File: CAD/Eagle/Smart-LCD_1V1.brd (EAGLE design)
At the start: 99 x 67.7 mm, 49 parts, among them Q121 MMBT2222AL, U101 MEGA8-P, U221 MCP4018T-104E/LT, U401 TS4871ID, X131 LDR, X141 Switches, X151 LEDs, X201 LCD_23WAY__UC1608, X231 LED_A, X232 LED_K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

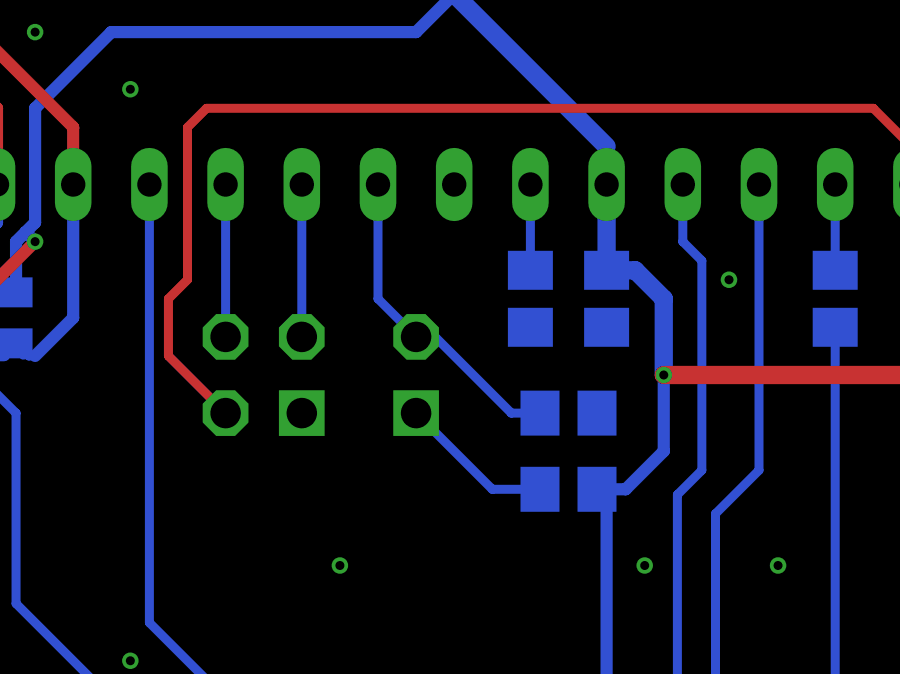
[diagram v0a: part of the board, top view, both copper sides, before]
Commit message: CAD - new version V1.1 - missing resistor for LDR added, missing header pin number 1 marking added
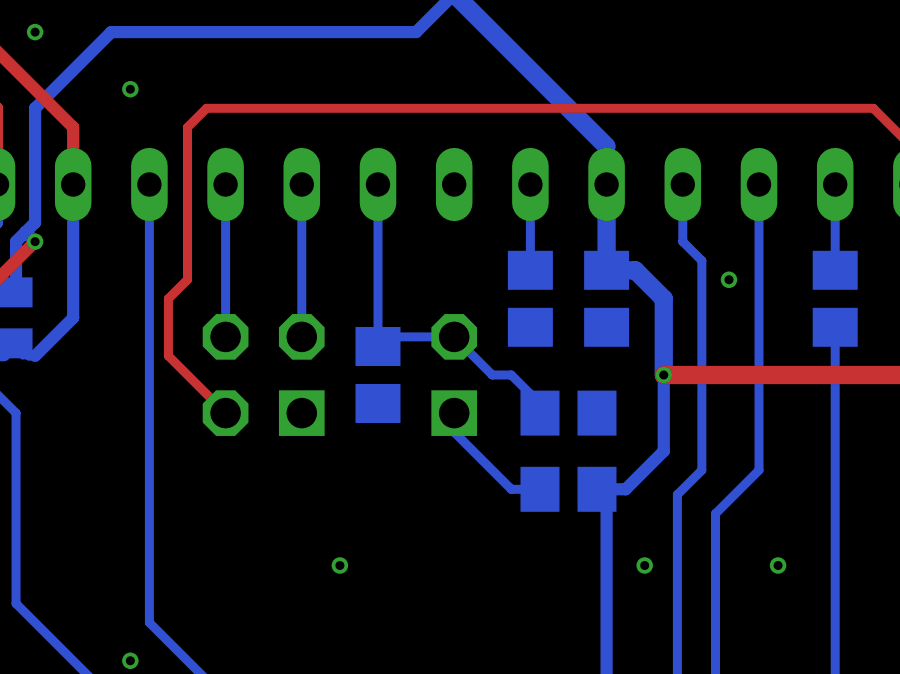
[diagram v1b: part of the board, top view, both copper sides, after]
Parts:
- added R132: 5.6kR, rcl:R0805
- moved X131 1.27 mm to (48.3, 26.0)
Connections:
- net GND: now also R132.2
- net LDR: now also R132.1
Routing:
- net LDR_P: track 5.18 -> 4.28 mm
- net LDR: track 10.8 -> 11.7 mm
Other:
- board text added: "1"
- board text added: "Smart-LCD V1.1 by DF4IAH"
- board text removed: "Smart-LCD V1.0 by DF4IAH"
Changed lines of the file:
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@@
 <dimension x1="0" y1="0" x2="0" y2="67.7" x3="-8.5" y3="33.85" textsize="1.016" layer="47"/>
 <dimension x1="0" y1="67.7" x2="99" y2="67.7" x3="49.5" y3="76.015" textsize="1.016" layer="47"/>
-<text x="27.94" y="62.865" size="1.4224" layer="22" ratio="15" rot="MR0">Smart-LCD V1.0
+<text x="27.94" y="62.865" size="1.4224" layer="22" ratio="15" rot="MR0">Smart-LCD V1.1
 by DF4IAH</text>
 <text x="48.26" y="22.86" size="1.016" layer="26" ratio="12" rot="MR0">LDR</text>
@@
 <dimension x1="0" y1="0" x2="0" y2="7.5" x3="-3.5" y3="3.75" textsize="0.6096" layer="47"/>
 <text x="97.155" y="29.845" size="1.016" layer="26" ratio="12" rot="MR0">Audio</text>
+<text x="52.07" y="65.405" size="0.6096" layer="22" ratio="20" rot="MR0">1</text>
+<text x="39.37" y="59.69" size="0.6096" layer="22" ratio="20" rot="MR0">1</text>
+<text x="92.71" y="36.83" size="0.6096" layer="22" ratio="20" rot="MR0">1</text>
+<text x="49.53" y="24.13" size="0.6096" layer="22" ratio="20" rot="MR0">1</text>
+<text x="43.815" y="24.13" size="0.6096" layer="22" ratio="20" rot="MR0">1</text>
 </plain>
 <attributes>
@@
 </class>
 </classes>
-<designrules name="Smart-LCD_1V0 *">
+<designrules name="Smart-LCD_1V1">
 <description language="de">
 &lt;p&gt;
@@
 </element>
 <element name="R222" library="rcl" package="R0805" value="650kR" x="30.48" y="24.765" smashed="yes" rot="MR0">
-<attribute name="NAME" x="34.925" y="24.765" size="0.6096" layer="26" rot="MR0"/>
+<attribute name="NAME" x="31.75" y="22.86" size="0.6096" layer="26" rot="MR0"/>
 <attribute name="VALUE" x="31.75" y="24.13" size="0.6096" layer="28" rot="MR0"/>
 </element>
@@
 </element>
 <element name="C102" library="rcl" package="C0805" value="100nF" x="53.34" y="29.845" smashed="yes" rot="MR270">
-<attribute name="NAME" x="54.61" y="27.94" size="0.6096" layer="26" rot="MR90"/>
+<attribute name="NAME" x="54.61" y="28.575" size="0.6096" layer="26" rot="MR90"/>
 <attribute name="VALUE" x="53.975" y="31.115" size="0.6096" layer="28" rot="MR270"/>
 </element>
@@
 <attribute name="VALUE" x="73.025" y="0.635" size="0.6096" layer="28" rot="MR90"/>
 </element>
-<element name="X131" library="df4iah_connector" package="1X02" value="LDR" x="46.99" y="26.035" smashed="yes" rot="MR0">
+<element name="X131" library="df4iah_connector" package="1X02" value="LDR" x="48.26" y="26.035" smashed="yes" rot="MR0">
 <attribute name="NAME" x="48.26" y="30.48" size="1.016" layer="26" ratio="10" rot="MR0"/>
-<attribute name="VALUE" x="46.99" y="27.94" size="0.6096" layer="28" rot="MR270"/>
+<attribute name="VALUE" x="48.26" y="27.94" size="0.6096" layer="28" rot="MR270"/>
 </element>
 <element name="R131" library="rcl" package="R0805" value="33kR" x="52.07" y="23.495" smashed="yes" rot="MR0">
-<attribute name="NAME" x="53.975" y="21.59" size="0.6096" layer="26" rot="MR0"/>
+<attribute name="NAME" x="53.34" y="21.59" size="0.6096" layer="26" rot="MR0"/>
 <attribute name="VALUE" x="53.34" y="22.86" size="0.6096" layer="28" rot="MR0"/>
 </element>
@@
 </element>
 <element name="X141" library="df4iah_connector" package="2X02" value="Switches" x="41.91" y="27.305" smashed="yes" rot="MR0">
-<attribute name="NAME" x="43.815" y="30.48" size="1.016" layer="26" ratio="10" rot="MR0"/>
+<attribute name="NAME" x="43.18" y="30.48" size="1.016" layer="26" ratio="10" rot="MR0"/>
 <attribute name="VALUE" x="43.18" y="26.67" size="0.6096" layer="28" rot="MR0"/>
 </element>
@@
 <attribute name="NAME" x="77.47" y="42.545" size="0.6096" layer="26" rot="MR0"/>
 <attribute name="VALUE" x="74.93" y="41.275" size="0.6096" layer="28" rot="MR180"/>
+</element>
+<element name="R132" library="rcl" package="R0805" value="5.6kR" x="45.72" y="27.305" smashed="yes" rot="MR270">
+<attribute name="NAME" x="46.355" y="24.13" size="0.6096" layer="26" rot="MR0"/>
+<attribute name="VALUE" x="48.26" y="27.94" size="1.27" layer="28" rot="MR270"/>
 </element>
 </elements>
@@
 <via x="66.04" y="66.04" extent="1-16" drill="0.3"/>
 <via x="43.815" y="61.595" extent="1-16" drill="0.3"/>
+<contactref element="R132" pad="2"/>
 </signal>
 <signal name="+5V">
@@
 <wire x1="35.56" y1="57.785" x2="34.925" y2="58.42" width="0.4064" layer="16"/>
 <contactref element="X231" pad="2"/>
+<wire x1="19.35" y1="2.505" x2="19.35" y2="2.505" width="0" layer="19" extent="1-16"/>
 </signal>
 <signal name="+3V3">
@@
 <wire x1="79.315" y1="2.54" x2="79.35" y2="2.505" width="0.8128" layer="16"/>
 <contactref element="X232" pad="2"/>
+<wire x1="79.35" y1="2.505" x2="79.35" y2="2.505" width="0" layer="19" extent="1-16"/>
 </signal>
 <signal name="LDR">
@@
 <contactref element="X131" pad="2"/>
 <contactref element="U101" pad="23"/>
-<wire x1="45.72" y1="33.655" x2="45.72" y2="29.845" width="0.3" layer="16"/>
-<wire x1="45.72" y1="29.845" x2="46.99" y2="28.575" width="0.3" layer="16"/>
-<wire x1="46.99" y1="28.575" x2="47.625" y2="28.575" width="0.3" layer="16"/>
-<wire x1="47.625" y1="28.575" x2="50.165" y2="26.035" width="0.3" layer="16"/>
-<wire x1="50.165" y1="26.035" x2="51.12" y2="26.035" width="0.3" layer="16"/>
+<wire x1="45.72" y1="33.655" x2="45.72" y2="28.575" width="0.3" layer="16"/>
+<wire x1="45.72" y1="28.575" x2="48.26" y2="28.575" width="0.3" layer="16"/>
+<wire x1="48.26" y1="28.575" x2="49.53" y2="27.305" width="0.3" layer="16"/>
+<wire x1="49.53" y1="27.305" x2="50.165" y2="27.305" width="0.3" layer="16"/>
+<wire x1="50.165" y1="27.305" x2="50.8" y2="26.67" width="0.3" layer="16"/>
+<wire x1="50.8" y1="26.67" x2="51.12" y2="26.035" width="0.3" layer="16"/>
+<contactref element="R132" pad="1"/>
+<wire x1="45.72" y1="28.255" x2="45.72" y2="28.575" width="0" layer="19" extent="16-16"/>
 </signal>
 <signal name="LDR_P">
 <contactref element="X131" pad="1"/>
 <contactref element="R131" pad="2"/>
-<wire x1="51.12" y1="23.495" x2="49.53" y2="23.495" width="0.3" layer="16"/>
-<wire x1="49.53" y1="23.495" x2="46.99" y2="26.035" width="0.3" layer="16"/>
+<wire x1="51.12" y1="23.495" x2="50.165" y2="23.495" width="0.3" layer="16"/>
+<wire x1="50.165" y1="23.495" x2="48.26" y2="25.4" width="0.3" layer="16"/>
+<wire x1="48.26" y1="25.4" x2="48.26" y2="26.035" width="0.3" layer="16"/>
 </signal>
 <signal name="AR_D">

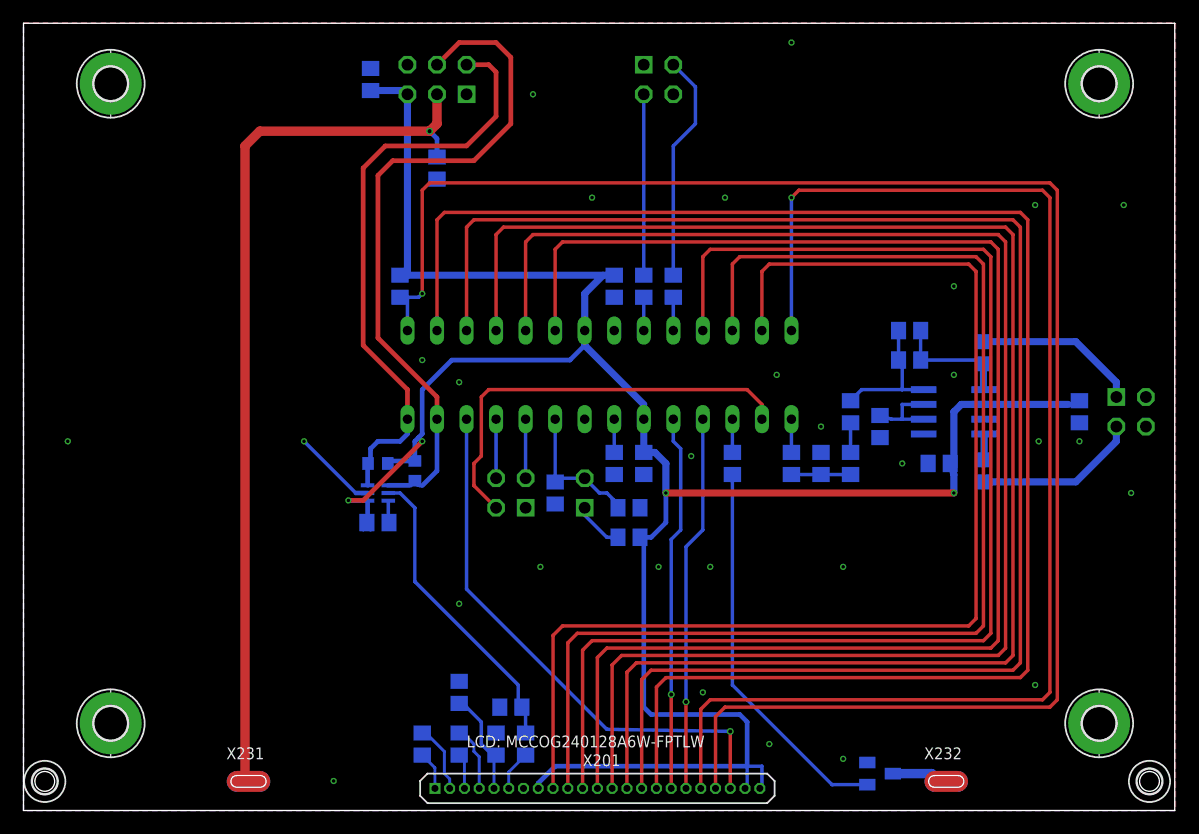
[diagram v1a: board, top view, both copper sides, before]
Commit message: CAD - four fiducials added
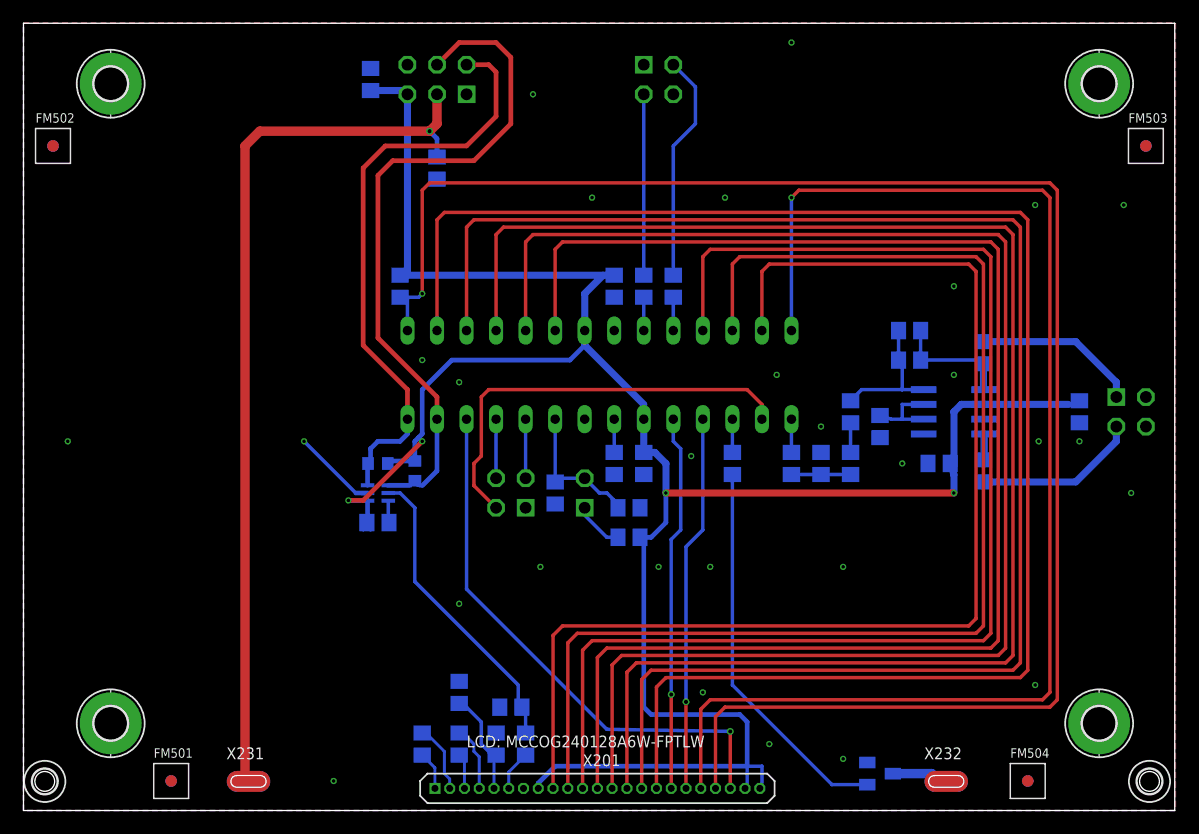
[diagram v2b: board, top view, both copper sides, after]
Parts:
- added FM501, FM502, FM503, FM504: FIDUCIAL_MARK_1MM, df4iah_fiducial:FIDUCIAL_MARK_1MM
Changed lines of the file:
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@@
 <attribute name="VALUE" x="48.26" y="27.94" size="1.27" layer="28" rot="MR270"/>
 </element>
+<element name="FM502" library="df4iah_fiducial" package="FIDUCIAL_MARK_1MM" value="FIDUCIAL_MARK_1MM" x="2.54" y="57.15" locked="yes"/>
+<element name="FM501" library="df4iah_fiducial" package="FIDUCIAL_MARK_1MM" value="FIDUCIAL_MARK_1MM" x="12.7" y="2.54" locked="yes"/>
+<element name="FM503" library="df4iah_fiducial" package="FIDUCIAL_MARK_1MM" value="FIDUCIAL_MARK_1MM" x="96.52" y="57.15" locked="yes"/>
+<element name="FM504" library="df4iah_fiducial" package="FIDUCIAL_MARK_1MM" value="FIDUCIAL_MARK_1MM" x="86.36" y="2.54" locked="yes"/>
 </elements>
 <signals>
